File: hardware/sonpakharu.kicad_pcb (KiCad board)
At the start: 2 copper layers, 1 part, among them IC1 ESP32-S3-WROOM-1U-N4

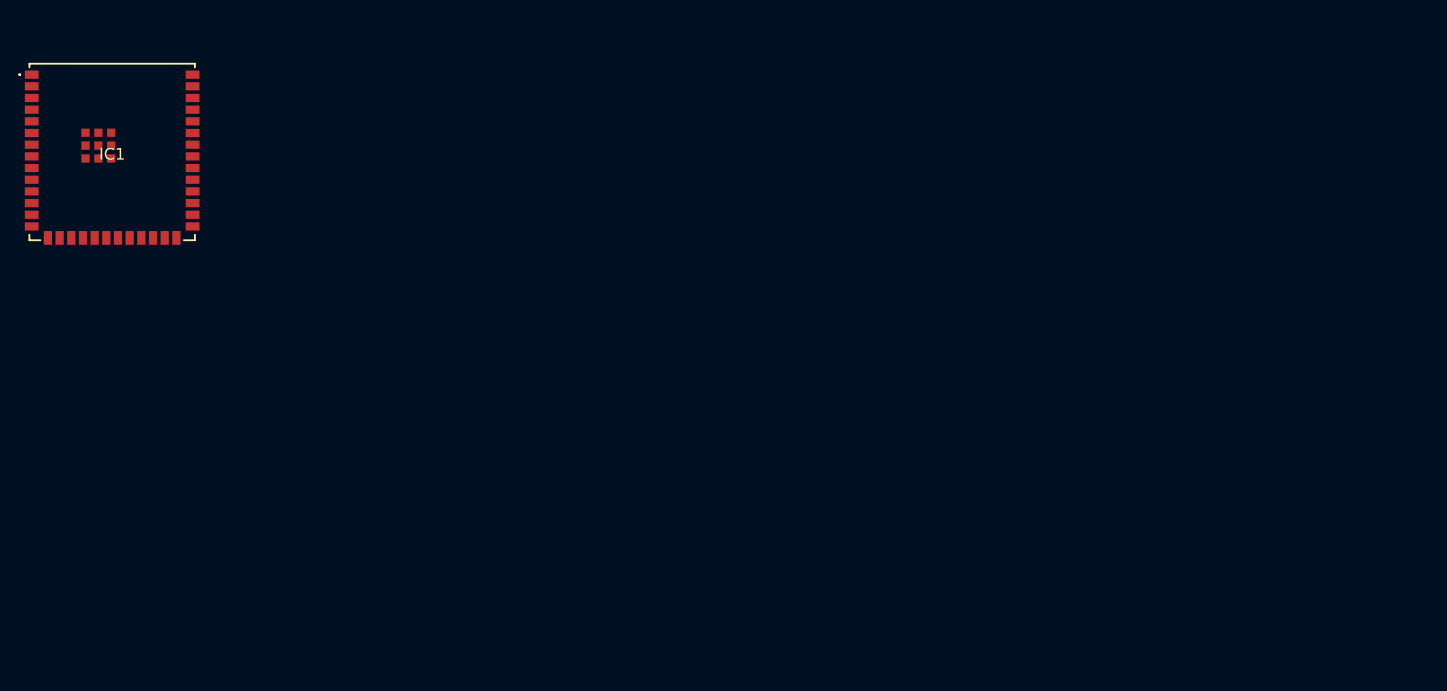
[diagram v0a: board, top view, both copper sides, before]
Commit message: Fix: routing
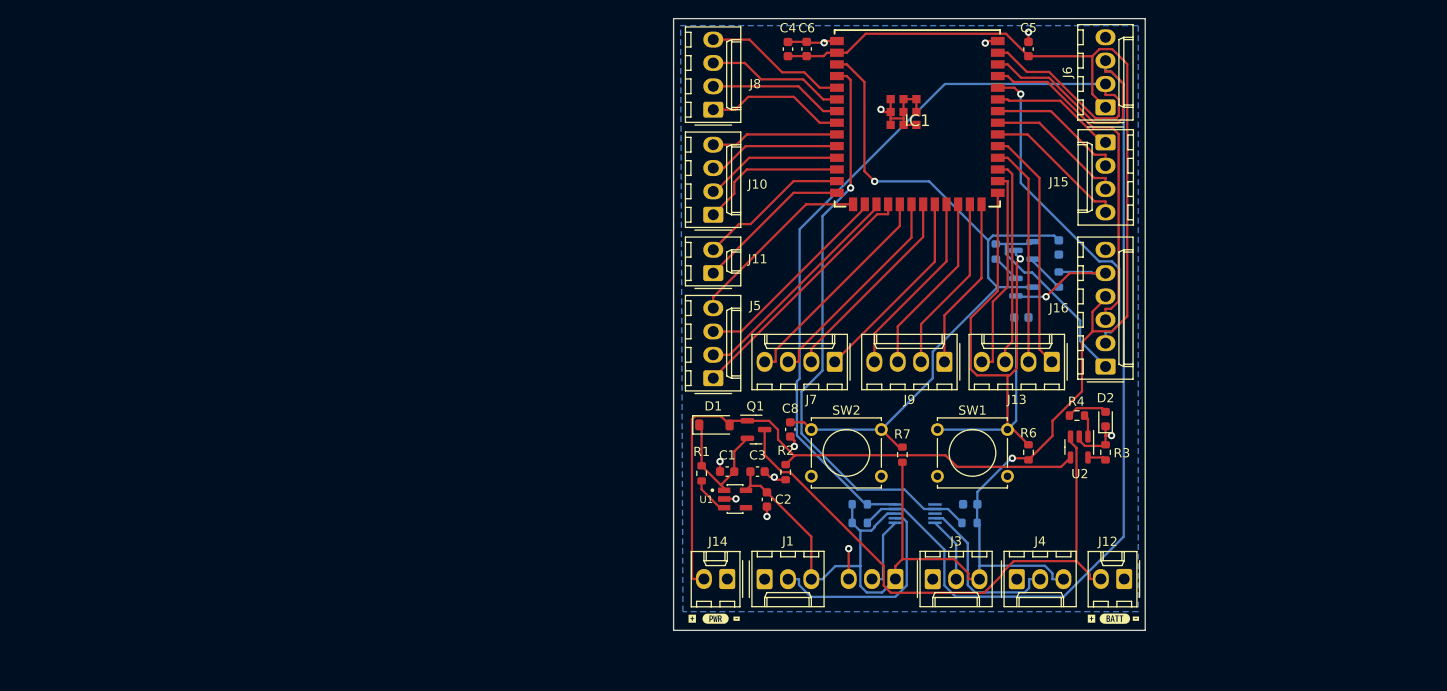
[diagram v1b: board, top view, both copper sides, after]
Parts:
- added C1: 10uF, Capacitor_SMD:C_0603_1608Metric, F.Cu at (111.7, 86.9)
- added C10: 1uF, Capacitor_SMD:C_0603_1608Metric, B.Cu at (138.2, 90.4)
- added C2: 10uF, Capacitor_SMD:C_0603_1608Metric, F.Cu at (116.1, 89.9)
- added C3: 10uF, Capacitor_SMD:C_0603_1608Metric, F.Cu at (115.0, 86.9)
- added C4: 10uF, Capacitor_SMD:C_0603_1608Metric, F.Cu at (118.4, 40.9)
- added C5: 10uF, Capacitor_SMD:C_0603_1608Metric, F.Cu at (144.5, 40.9)
- added C6: 1uF, Capacitor_SMD:C_0603_1608Metric, F.Cu at (120.4, 40.9)
- added C7: 4.7uF, Capacitor_SMD:C_0603_1608Metric, B.Cu at (147.8, 62.5)
- added C8: 1uF, Capacitor_SMD:C_0603_1608Metric, F.Cu at (118.6, 82.3)
- added C9: 1uF, Capacitor_SMD:C_0603_1608Metric, B.Cu at (143.8, 70.1)
- added D1: MBR0540, Diode_SMD:D_SOD-123, F.Cu at (110.4, 81.8)
- added D2: orange, LED_SMD:LED_0603_1608Metric, F.Cu at (152.9, 81.2)
- added J1: ADC4, Connector_Molex:Molex_KK-254_AE-6410-03A_1x03_P2.54mm_Vertical, F.Cu at (115.8, 98.6)
- added J10: EXT2, Connector_Molex:Molex_KK-254_AE-6410-04A_1x04_P2.54mm_Vertical, F.Cu at (110.2, 58.9)
- added J11: EXT3, Connector_Molex:Molex_KK-254_AE-6410-02A_1x02_P2.54mm_Vertical, F.Cu at (110.2, 65.3)
- added J12: BATT, Connector_Molex:Molex_KK-254_AE-6410-02A_1x02_P2.54mm_Vertical, F.Cu at (154.9, 98.6)
- added J13: EXT7, Connector_Molex:Molex_KK-254_AE-6410-04A_1x04_P2.54mm_Vertical, F.Cu at (147.1, 74.9)
- added J14: PWR, Connector_Molex:Molex_KK-254_AE-6410-02A_1x02_P2.54mm_Vertical, F.Cu at (111.8, 98.6)
- added J15: EXT8, Connector_Molex:Molex_KK-254_AE-6410-04A_1x04_P2.54mm_Vertical, F.Cu at (152.9, 51.1)
- added J16: FTDI, Connector_Molex:Molex_KK-254_AE-6410-06A_1x06_P2.54mm_Vertical, F.Cu at (152.9, 75.4)
- added J2: ADC3, Connector_Molex:Molex_KK-254_AE-6410-03A_1x03_P2.54mm_Vertical, B.Cu at (130.0, 98.6)
- added J3: ADC2, Connector_Molex:Molex_KK-254_AE-6410-03A_1x03_P2.54mm_Vertical, F.Cu at (134.1, 98.6)
- added J4: ADC1, Connector_Molex:Molex_KK-254_AE-6410-03A_1x03_P2.54mm_Vertical, F.Cu at (143.3, 98.6)
- added J5: EXT4, Connector_Molex:Molex_KK-254_AE-6410-04A_1x04_P2.54mm_Vertical, F.Cu at (110.2, 76.7)
- added J6: I2C, Connector_Molex:Molex_KK-254_AE-6410-04A_1x04_P2.54mm_Vertical, F.Cu at (152.9, 47.2)
- added J7: EXT5, Connector_Molex:Molex_KK-254_AE-6410-04A_1x04_P2.54mm_Vertical, F.Cu at (123.4, 74.9)
- added J8: EXT1, Connector_Molex:Molex_KK-254_AE-6410-04A_1x04_P2.54mm_Vertical, F.Cu at (110.2, 47.5)
- added J9: EXT6, Connector_Molex:Molex_KK-254_AE-6410-04A_1x04_P2.54mm_Vertical, F.Cu at (135.4, 74.9)
- added Q1: DMG3415U, Package_TO_SOT_SMD:SOT-23, F.Cu at (114.9, 82.3)
- added Q2: S8050, Package_TO_SOT_SMD:SOT-23, B.Cu at (144.1, 66.8)
- added Q3: S8050, Package_TO_SOT_SMD:SOT-23, B.Cu at (144.1, 62.8)
- added R1: 100K, Resistor_SMD:R_0603_1608Metric, F.Cu at (109.0, 87.1)
- added R10: 10K, Resistor_SMD:R_0603_1608Metric, B.Cu at (126.2, 92.5)
- added R11: 10K, Resistor_SMD:R_0603_1608Metric, B.Cu at (138.1, 92.5)
- added R2: 100K, Resistor_SMD:R_0603_1608Metric, F.Cu at (118.1, 86.9)
- added R3: 5.1K, Resistor_SMD:R_0603_1608Metric, F.Cu at (152.9, 84.8)
- added R4: 5.1K, Resistor_SMD:R_0603_1608Metric, F.Cu at (149.8, 80.8)
- added R5: 12K, Resistor_SMD:R_0603_1608Metric, B.Cu at (141.0, 62.9)
- added R6: 10K, Resistor_SMD:R_0603_1608Metric, F.Cu at (144.5, 84.8)
- added R7: 10K, Resistor_SMD:R_0603_1608Metric, F.Cu at (130.8, 85.0)
- added R8: 12K, Resistor_SMD:R_0603_1608Metric, B.Cu at (147.8, 66.0)
- added R9: 10K, Resistor_SMD:R_0603_1608Metric, B.Cu at (126.2, 90.4)
- added SW1: Boot, Button_Switch_THT:SW_Tactile_Straight_KSA0Axx1LFTR, F.Cu at (134.6, 82.3)
- added SW2: Reset, Button_Switch_THT:SW_Tactile_Straight_KSA0Axx1LFTR, F.Cu at (120.9, 82.3)
- added U1: AP2112K-3.3TRG1, AP2112K-3.3TRG1:SOT95P285X140-5N, F.Cu at (112.6, 89.8)
- added U2: MCP73831-2-OT, Package_TO_SOT_SMD:SOT-23-5, F.Cu at (150.0, 84.2)
- added U3: ADS1115IDGSR, ADS1115IDGSR:SOP50P490X110-10N, B.Cu at (132.2, 91.4)
- added kibuzzard-6592A779: G***, kibuzzard-6592A779, F.Cu at (110.5, 102.9)
- added kibuzzard-6592A784: G***, kibuzzard-6592A784, F.Cu at (153.9, 102.9)
- added kibuzzard-6592A79E: G***, kibuzzard-6592A79E, F.Cu at (108.0, 102.9)
- added kibuzzard-6592A7AE: G***, kibuzzard-6592A7AE, F.Cu at (112.8, 102.9)
- added kibuzzard-6592A7C7: G***, kibuzzard-6592A7C7, F.Cu at (151.4, 102.9)
- added kibuzzard-6592AE79: G***, kibuzzard-6592AE79, F.Cu at (156.2, 102.9)
- IC1: footprint KiCad:ESP32S3WROOM1UN4 -> RF_Module:ESP32S3WROOM1UN4
- moved IC1 87.7 mm to (132.4, 48.4)
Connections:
- IC1 pad 1: unconnected-(IC1-GND_1-Pad1) -> GND
- IC1 pad 10: unconnected-(IC1-IO17-Pad10) -> /GP6
- IC1 pad 11: unconnected-(IC1-IO18-Pad11) -> /GP7
- IC1 pad 12: unconnected-(IC1-IO8-Pad12) -> /GP8
- IC1 pad 13: unconnected-(IC1-IO19-Pad13) -> /GP9
- IC1 pad 14: unconnected-(IC1-IO20-Pad14) -> /GP10
- IC1 pad 15: unconnected-(IC1-IO3-Pad15) -> /GP11
- IC1 pad 16: unconnected-(IC1-IO46-Pad16) -> /GP12
- IC1 pad 17: unconnected-(IC1-IO9-Pad17) -> /GP13
- IC1 pad 18: unconnected-(IC1-IO10-Pad18) -> /GP14
- IC1 pad 19: unconnected-(IC1-IO11-Pad19) -> /GP15
- IC1 pad 2: unconnected-(IC1-3V3-Pad2) -> +3V3
- IC1 pad 20: unconnected-(IC1-IO12-Pad20) -> /GP16
- IC1 pad 21: unconnected-(IC1-IO13-Pad21) -> /GP17
- IC1 pad 22: unconnected-(IC1-IO14-Pad22) -> /GP18
- IC1 pad 23: unconnected-(IC1-IO21-Pad23) -> /GP19
- IC1 pad 24: unconnected-(IC1-IO47-Pad24) -> /GP20
- IC1 pad 25: unconnected-(IC1-IO48-Pad25) -> /GP21
- IC1 pad 26: unconnected-(IC1-IO45-Pad26) -> /GP22
- IC1 pad 27: unconnected-(IC1-IO0-Pad27) -> /IO0
- IC1 pad 28: unconnected-(IC1-IO35-Pad28) -> /GP23
- IC1 pad 29: unconnected-(IC1-IO36-Pad29) -> /GP24
- IC1 pad 3: unconnected-(IC1-EN-Pad3) -> /EN
- IC1 pad 30: unconnected-(IC1-IO37-Pad30) -> /GP25
- IC1 pad 31: unconnected-(IC1-IO38-Pad31) -> /GP26
- IC1 pad 32: unconnected-(IC1-IO39-Pad32) -> /GP27
- IC1 pad 33: unconnected-(IC1-IO40-Pad33) -> /GP28
- IC1 pad 34: unconnected-(IC1-IO41-Pad34) -> /GP29
- IC1 pad 35: unconnected-(IC1-IO42-Pad35) -> /GP30
- IC1 pad 36: unconnected-(IC1-RXD0-Pad36) -> /RX
- IC1 pad 37: unconnected-(IC1-TXD0-Pad37) -> /TX
- IC1 pad 38: unconnected-(IC1-IO2-Pad38) -> /SDA
- IC1 pad 39: unconnected-(IC1-IO1-Pad39) -> /SCL
- IC1 pad 4: unconnected-(IC1-IO4-Pad4) -> /IO4
- IC1 pad 40: unconnected-(IC1-GND_2-Pad40) -> GND
- IC1 pad 41: unconnected-(IC1-GND_3-Pad41) -> GND
- IC1 pad 42: unconnected-(IC1-GND_4-Pad42) -> GND
- IC1 pad 43: unconnected-(IC1-GND_5-Pad43) -> GND
- IC1 pad 44: unconnected-(IC1-GND_6-Pad44) -> GND
- IC1 pad 45: unconnected-(IC1-GND_7-Pad45) -> GND
- IC1 pad 46: unconnected-(IC1-GND_8-Pad46) -> GND
- IC1 pad 47: unconnected-(IC1-GND_9-Pad47) -> GND
- IC1 pad 48: unconnected-(IC1-GND_10-Pad48) -> GND
- IC1 pad 49: unconnected-(IC1-GND_11-Pad49) -> GND
- IC1 pad 5: unconnected-(IC1-IO5-Pad5) -> /GP1
- IC1 pad 6: unconnected-(IC1-IO6-Pad6) -> /GP2
- IC1 pad 7: unconnected-(IC1-IO7-Pad7) -> /GP3
- IC1 pad 8: unconnected-(IC1-IO15-Pad8) -> /GP4
- IC1 pad 9: unconnected-(IC1-IO16-Pad9) -> /GP5
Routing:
- net +3V3: track 0.00 -> 192.4 mm, vias 0 -> 2
- net /SDA: track 0.00 -> 114.3 mm
- net /SCL: track 0.00 -> 97.1 mm
- net /EN: track 0.00 -> 81.6 mm, vias 0 -> 1
- net /IO0: track 0.00 -> 68.4 mm, vias 0 -> 1
- net VBUS: track 0.00 -> 65.0 mm
- net /IO4: track 0.00 -> 63.8 mm, vias 0 -> 1
- net +BATT: track 0.00 -> 63.3 mm
- net /TX: track 0.00 -> 36.9 mm
- net /RX: track 0.00 -> 36.1 mm, vias 0 -> 1
- net GND: track 0.00 -> 33.9 mm, vias 0 -> 10
- net /GP14: track 0.00 -> 27.5 mm
- net /GP26: track 0.00 -> 26.5 mm
- net /GP13: track 0.00 -> 24.8 mm
- net /GP25: track 0.00 -> 24.2 mm
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- added copper zone on B.Cu, net GND
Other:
- board outline added: 51.3 x 66.5 mm

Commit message: routing done
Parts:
- J2: moved to F.Cu
- moved J2 5.08 mm to (125.0, 98.6), turned to 0 degrees
- moved C7 0.51 mm to (148.3, 62.5)
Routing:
- net GND: track 33.9 -> 94.9 mm, vias 10 -> 17
- net /SDA: track 114.3 -> 86.1 mm
- net /IO4: track 63.8 -> 91.3 mm
- net /SCL: track 97.1 -> 87.4 mm
- net /IO0: track 68.4 -> 61.0 mm, vias 1 -> 0
- net /RTS: track 16.0 -> 11.0 mm, vias 1 -> 0
- net /RX: track 36.1 -> 40.8 mm, vias 1 -> 0
- net /DTR: track 22.5 -> 27.1 mm, vias 0 -> 1
- net Net-(Q3-B): track 4.21 -> 8.65 mm, vias 0 -> 2
- net /TX: track 36.9 -> 39.2 mm
- net +3V3: track 192.4 -> 193.6 mm, vias 2 -> 0
- net /GP4: track 15.2 -> 14.0 mm
- net /EN: track 81.6 -> 80.7 mm
- net /GP5: track 13.9 -> 14.7 mm
- net VBUS: track 65.0 -> 64.3 mm
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
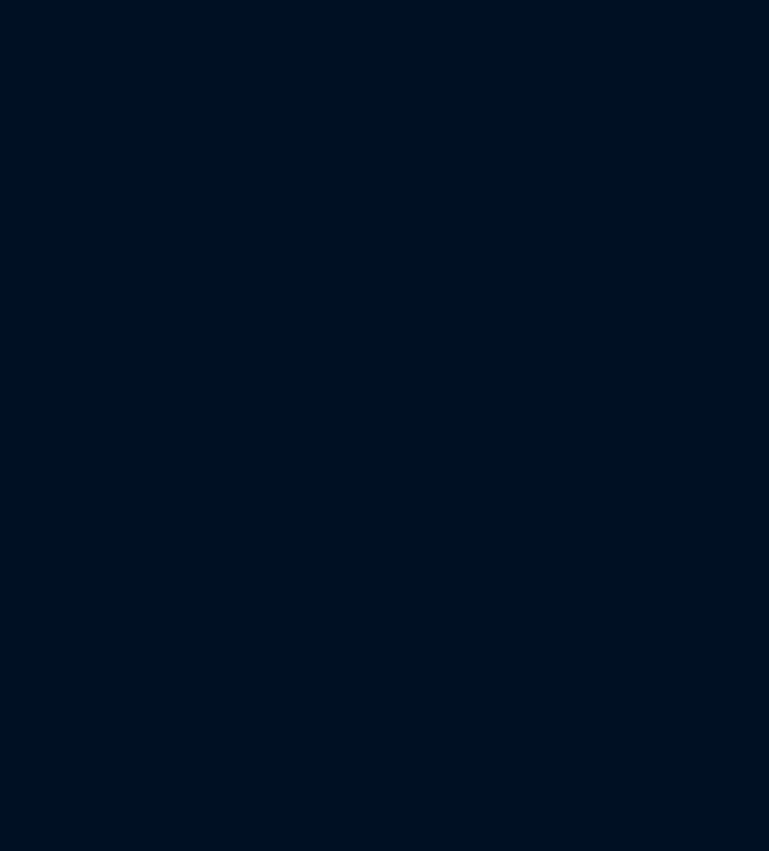
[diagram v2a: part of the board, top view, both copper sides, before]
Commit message: converted 485 sch to pcb
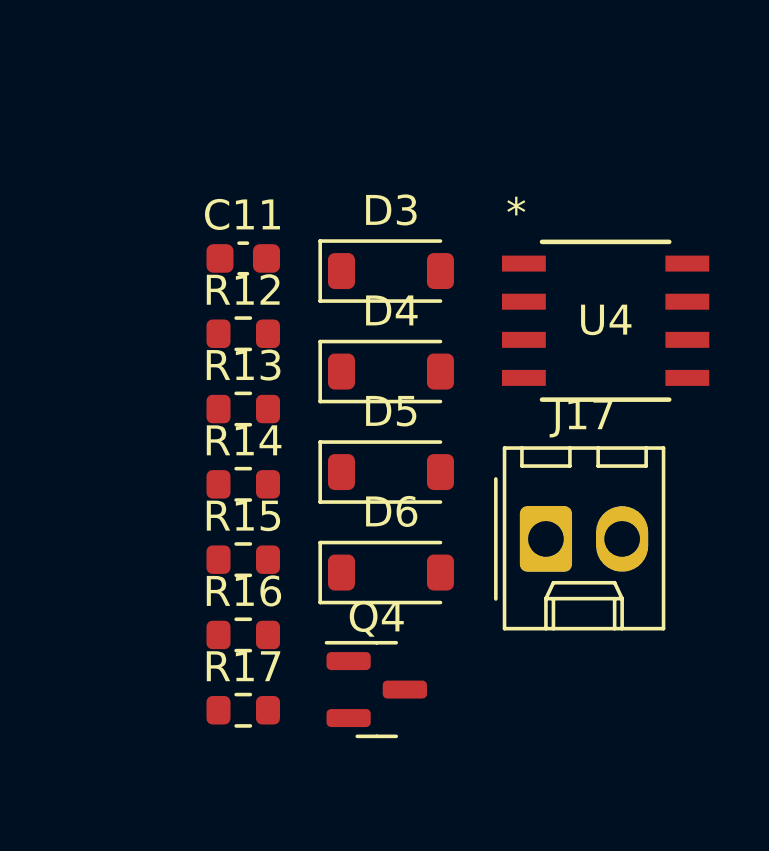
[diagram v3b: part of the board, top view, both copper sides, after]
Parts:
- added C11: 1uF, Capacitor_SMD:C_0603_1608Metric, F.Cu at (172.5, 86.4)
- added D3: MBR0540, Diode_SMD:D_SOD-123, F.Cu at (177.5, 86.8)
- added D4: MBR0540, Diode_SMD:D_SOD-123, F.Cu at (177.5, 90.2)
- added D5: MBR0540, Diode_SMD:D_SOD-123, F.Cu at (177.5, 93.5)
- added D6: MBR0540, Diode_SMD:D_SOD-123, F.Cu at (177.5, 96.9)
- added J17: 485, Connector_Molex:Molex_KK-254_AE-6410-02A_1x02_P2.54mm_Vertical, F.Cu at (182.6, 95.8)
- added Q4: S8050, Package_TO_SOT_SMD:SOT-23, F.Cu at (177.0, 100.8)
- added R12: 10K, Resistor_SMD:R_0603_1608Metric, F.Cu at (172.5, 88.9)
- added R13: 10K, Resistor_SMD:R_0603_1608Metric, F.Cu at (172.5, 91.4)
- added R14: 10K, Resistor_SMD:R_0603_1608Metric, F.Cu at (172.5, 93.9)
- added R15: 10K, Resistor_SMD:R_0603_1608Metric, F.Cu at (172.5, 96.4)
- added R16: 20K, Resistor_SMD:R_0603_1608Metric, F.Cu at (172.5, 99.0)
- added R17: 20K, Resistor_SMD:R_0603_1608Metric, F.Cu at (172.5, 101.5)
- added U4: MAX485E, MAX485SOIC8:21-0041B_8_MXM, F.Cu at (184.6, 88.5)

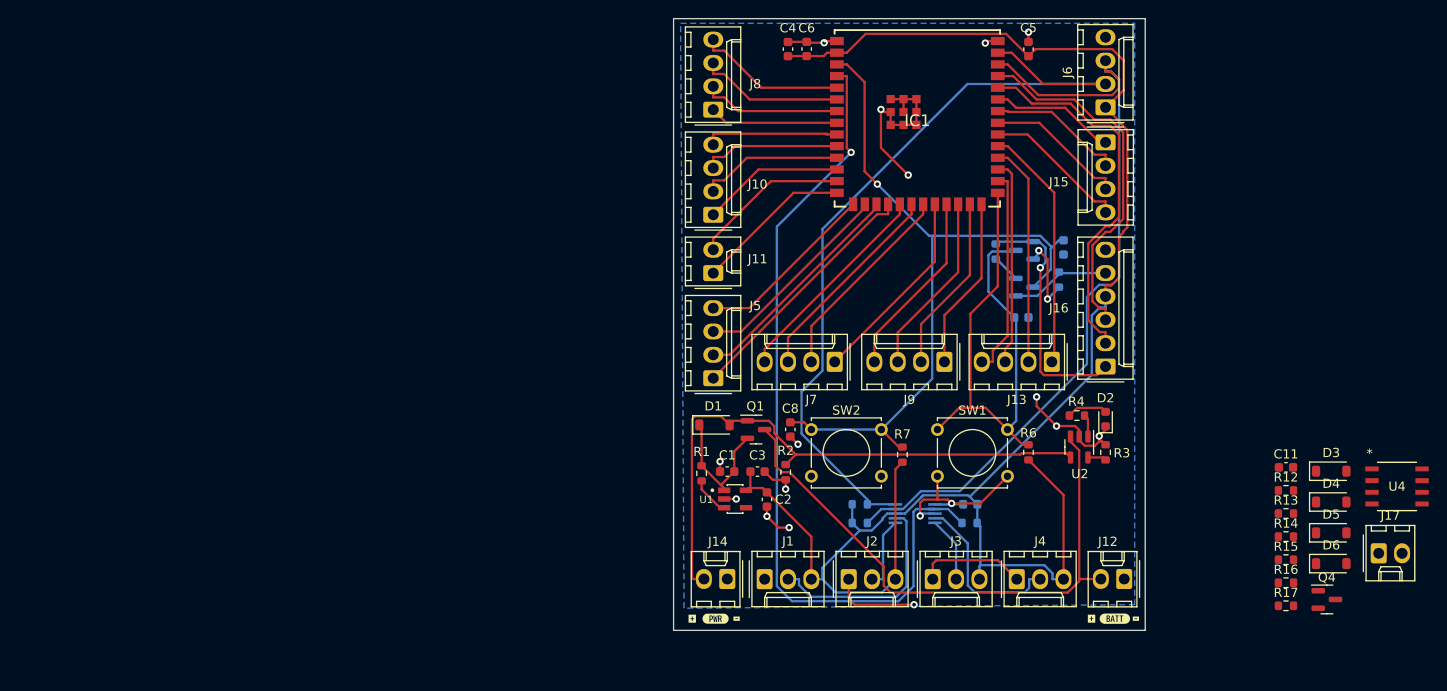
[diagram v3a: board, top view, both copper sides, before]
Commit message: component placment done
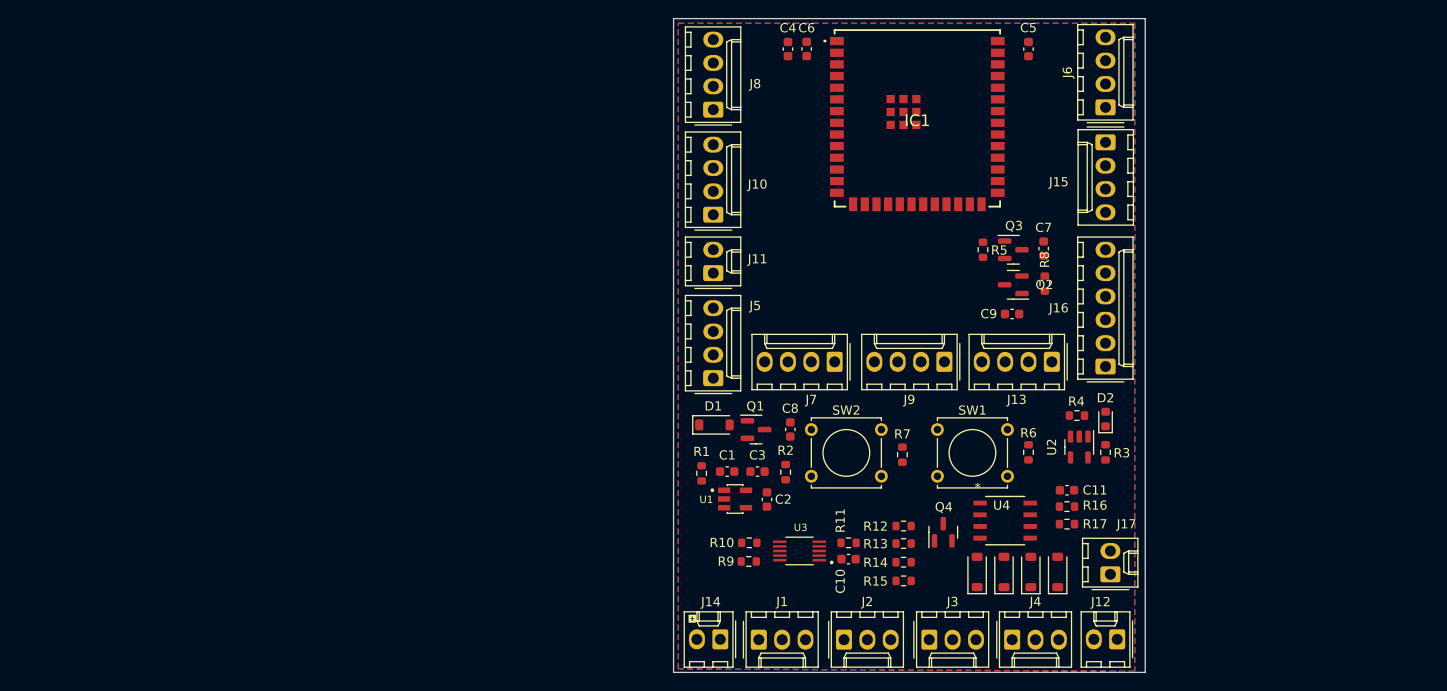
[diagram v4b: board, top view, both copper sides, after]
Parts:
- removed kibuzzard-6592A779: G***, kibuzzard-6592A779
- removed kibuzzard-6592A784: G***, kibuzzard-6592A784
- removed kibuzzard-6592A7AE: G***, kibuzzard-6592A7AE
- removed kibuzzard-6592A7C7: G***, kibuzzard-6592A7C7
- removed kibuzzard-6592AE79: G***, kibuzzard-6592AE79
- C10, C7, C9, Q2, Q3, R10, R11, R5, R8, R9, U3: moved to F.Cu
- moved U4 42.8 mm to (142.0, 92.2)
- moved Q4 42.4 mm to (135.3, 93.5), turned to 90 degrees
- moved R12 41.8 mm to (130.9, 92.8)
- moved R13 41.7 mm to (130.9, 94.7)
- moved R14 41.7 mm to (130.9, 96.7)
- moved R15 41.7 mm to (130.9, 98.8)
- moved D3 40.1 mm to (138.9, 97.8), turned to 90 degrees
- moved D4 36.4 mm to (141.9, 97.8), turned to 90 degrees
- moved D5 33.0 mm to (144.8, 97.8), turned to 90 degrees
- moved D6 29.8 mm to (147.7, 97.8), turned to 90 degrees
- moved J17 29.3 mm to (153.4, 98.0), turned to 90 degrees
- moved R17 25.4 mm to (148.7, 92.6)
- moved R16 25.2 mm to (148.7, 90.7), turned to 180 degrees
- moved C11 23.9 mm to (148.7, 88.9), turned to 180 degrees
- moved C10 14.5 mm to (125.0, 96.4)
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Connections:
- net Net-(D3-A) renamed /D+
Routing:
- net +3V3: track 193.6 -> 0.00 mm
- net GND: track 94.9 -> 0.00 mm, vias 17 -> 0
- net /IO4: track 91.3 -> 0.00 mm, vias 1 -> 0
- net /SCL: track 87.4 -> 0.00 mm
- net /SDA: track 86.1 -> 0.00 mm
- net /EN: track 80.7 -> 0.00 mm, vias 1 -> 0
- net VBUS: track 64.3 -> 0.00 mm
- net +BATT: track 63.4 -> 0.00 mm
- net /IO0: track 61.0 -> 0.00 mm
- net /RX: track 40.8 -> 0.00 mm
- net /TX: track 39.2 -> 0.00 mm
- net /GP14: track 27.5 -> 0.00 mm
- net /DTR: track 27.1 -> 0.00 mm, vias 1 -> 0
- net /GP26: track 26.8 -> 0.00 mm
- net /GP13: track 24.8 -> 0.00 mm
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- added copper zone on F.Cu, net GND
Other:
- board size 51.3 x 66.5 mm -> 51.3 x 71.1 mm
